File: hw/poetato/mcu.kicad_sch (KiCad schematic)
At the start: 106 parts, among them J3 FTSH-105-01-L-DV-007-K, J4 61300611121, J8 614105150721, Q10 NTK3134N, Q9 NTK3134N, U1 MCXN247VKLT, U10 SE051, U11 S25FL064LABMFI013, U18 TPS563252DRLR, U2 LP3470A293DBVR, U20 USBLC6-4, U8 USBLC6-4, U9 USBLC6-4, Y1 32.768kHz, Y3 24MHz

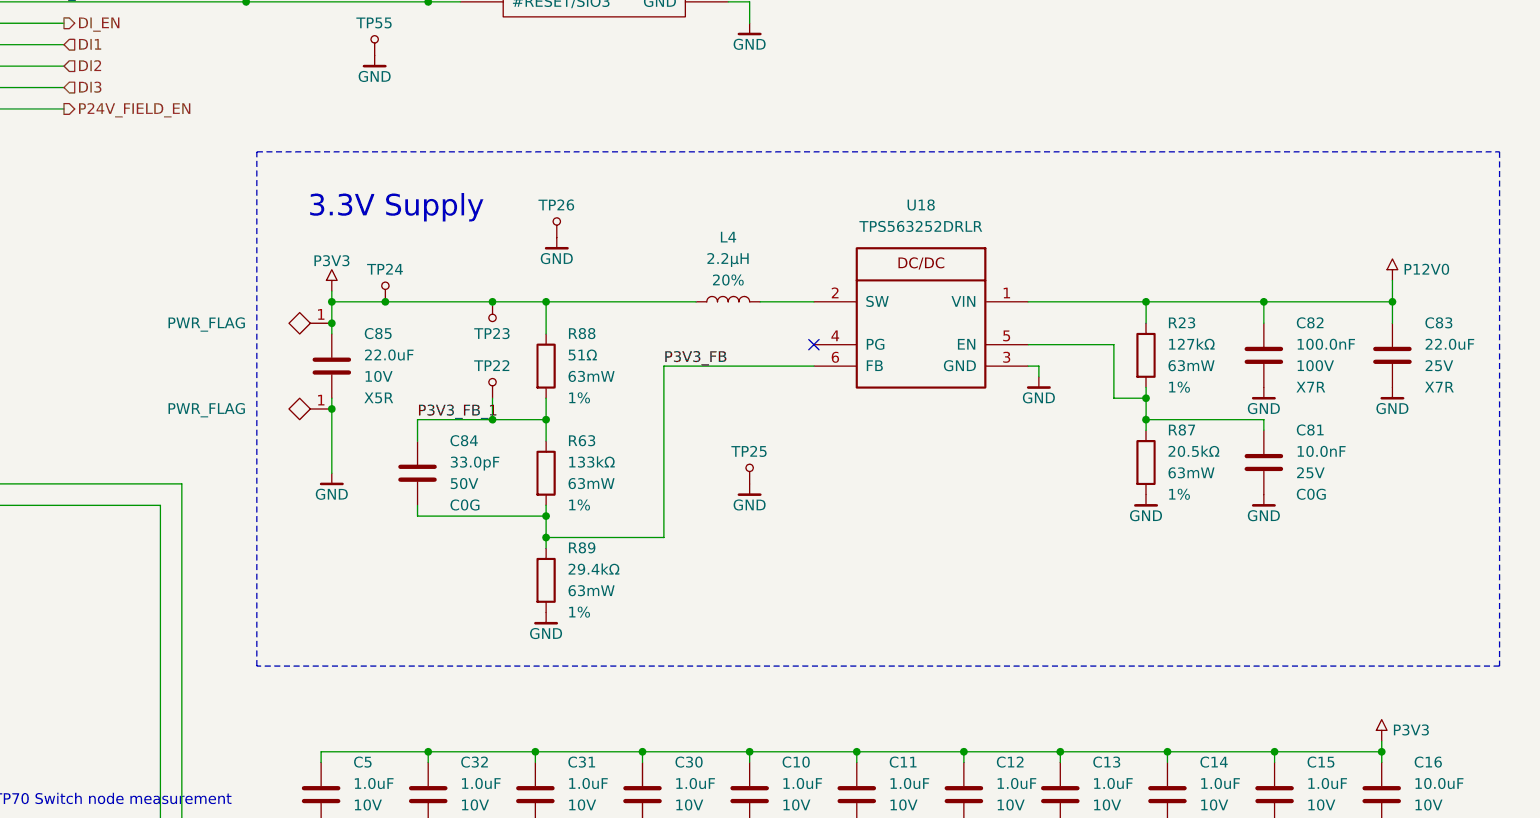
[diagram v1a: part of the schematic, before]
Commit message: hw: move the DC/DC converters to a new top-level Power sheet
power.kicad_sch (page 4) holds the 3.3 V buck (from MCU), the isolated
24 V field supply with its enable FET and LED (from IO) and the RS-485
5 V buck (from RS485). The two bucks are mirrored to read left to right.
The PoE flyback stays on the Ethernet sheet.

P5V_RS485 is now a power symbol and P24V_FIELD_EN goes from MCU to the
Power sheet at the top level. On IO the eFuse moved next to J1, removing
the output loop around the page. The power tree is redrawn more compact
to make room for the new sheet symbol.

Symbols keep their UUIDs and references. ERC clean; every net connects
the same pins as before, 7 nets renamed by the new sheet path.
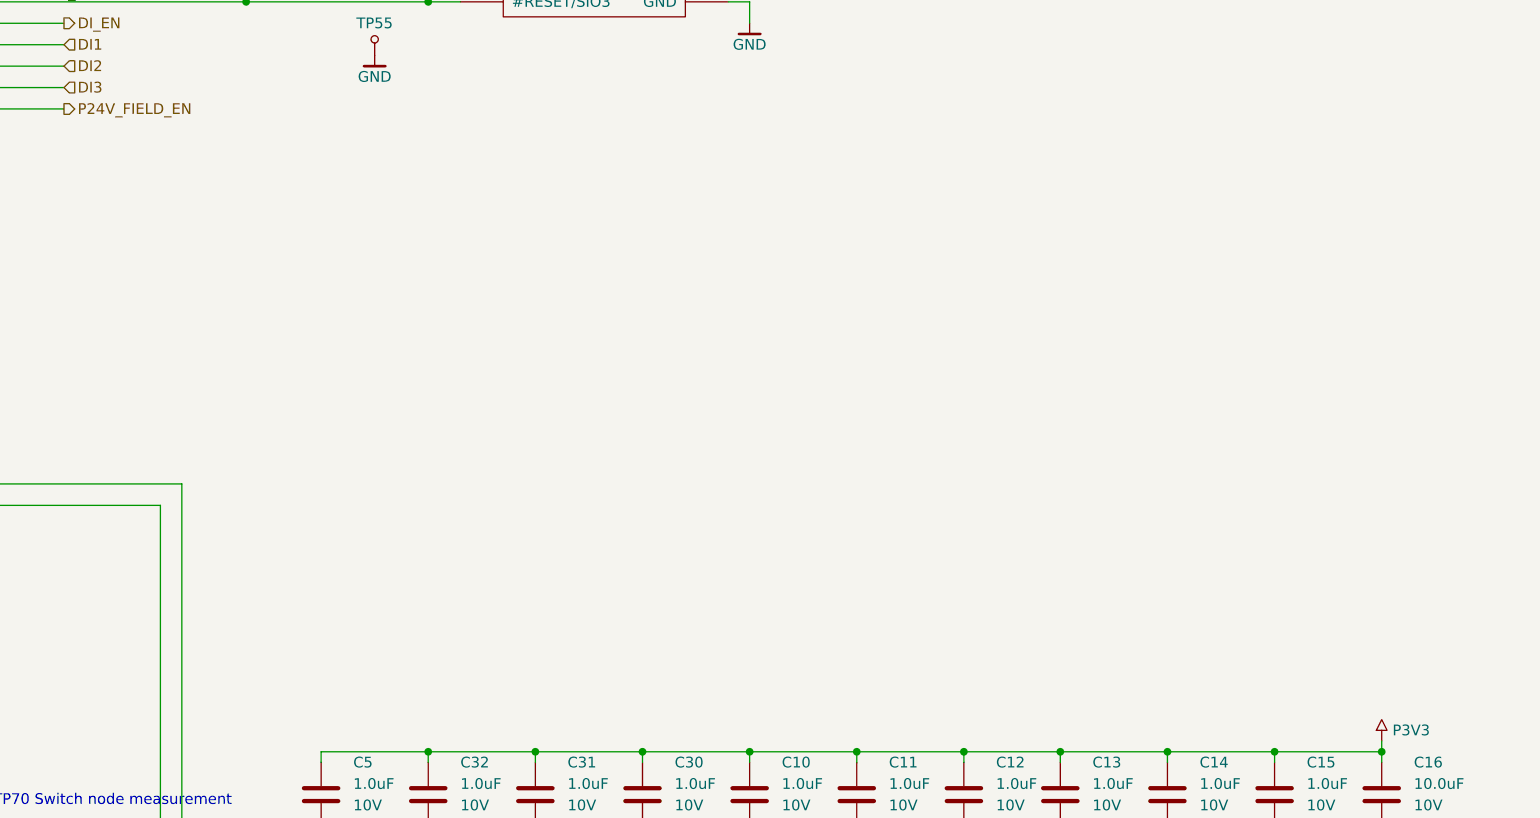
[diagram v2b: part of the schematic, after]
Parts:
- removed C81: ${Capacitance}, Capacitor_SMD:C_0402_1005Metric, symbol cap_mlcc_murata_GRM:GRM/C0402_10n_25V_C0G_5%
- removed C82: ${Capacitance}, Capacitor_SMD:C_0603_1608Metric, symbol cap_mlcc_murata_GRM:GRM/C0603_100n_100V_X7R_10%
- removed C83: ${Capacitance}, Capacitor_SMD:C_1210_3225Metric, symbol cap_mlcc_murata_GRM:GRM/C1210_22u_25V_X7R_10%
- removed C84: ${Capacitance}, Capacitor_SMD:C_0402_1005Metric, symbol cap_mlcc_murata_GRM:GRM/C0402_33p_50V_C0G_2%
- removed C85: ${Capacitance}, Capacitor_SMD:C_0603_1608Metric, symbol cap_mlcc_murata_GRM:GRM/C0603_22u_10V_X5R_20%
- removed L4: 2.2µH, Jonas:IHLP1212BZ, symbol ind_power_vishay_ihlp:IHLP/L1212_2u2_20_5A7
- removed R23: 127kΩ, Resistor_SMD:R_0402_1005Metric, symbol res_chip_vishay_crcw:CRCW/R0402_127k0_1_63mW
- removed R63: 133kΩ, Resistor_SMD:R_0402_1005Metric, symbol res_chip_vishay_crcw:CRCW/R0402_133k0_1_63mW
- removed R87: 20.5kΩ, Resistor_SMD:R_0402_1005Metric, symbol res_chip_vishay_crcw:CRCW/R0402_20k5_1_63mW
- removed R88: 51Ω, Resistor_SMD:R_0402_1005Metric, symbol res_chip_vishay_crcw:CRCW/R0402_51R0_1_63mW
- removed R89: 29.4kΩ, Resistor_SMD:R_0402_1005Metric, symbol res_chip_vishay_crcw:CRCW/R0402_29k4_1_63mW
- removed TP22, TP23, TP24, TP25, TP26: TP, TestPoint:TestPoint_Pad_D1.0mm, symbol power:TP
- removed U18: TPS563252DRLR, Package_TO_SOT_SMD:SOT-563, symbol dcdc:TPS563252DRLR
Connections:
- no-connect marks 46 -> 45
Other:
- note removed: "3.3V Supply"
- title: PoEtato - MCU, secure element, flash and 3.3 V supply -> PoEtato - MCU, secure element and flash
